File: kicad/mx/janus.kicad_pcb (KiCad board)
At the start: 2 copper layers, 95 x 95 mm, 62 parts, among them J1 8P8C Double Sided, SW1 SW_Push, SW10 SW_Push, SW11 SW_Push, SW12 SW_Push, SW13 SW_Push, SW14 SW_Push, SW15 SW_Push, SW16 SW_Push, SW17 SW_Push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

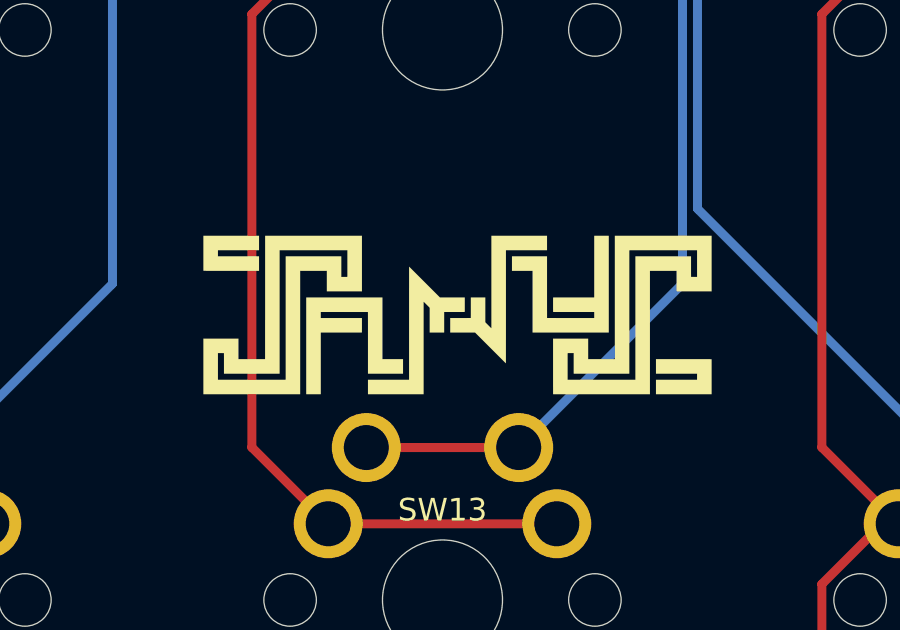
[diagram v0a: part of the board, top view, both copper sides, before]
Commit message: Center silkscreen logo
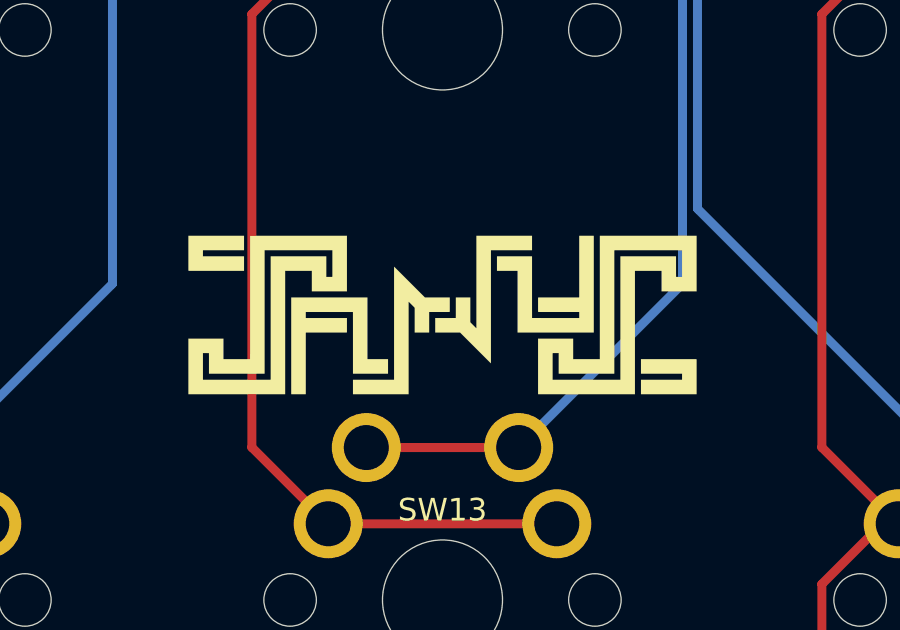
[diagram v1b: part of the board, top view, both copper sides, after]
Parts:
- moved LOGO1 0.50 mm to (148.5, 105.0)
- moved LOGO2 0.50 mm to (148.5, 105.0)
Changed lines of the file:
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@@
   )
   (footprint "janus-footprints:Logo_Janus" (layer "F.Cu")
-    (at 149 105 -45)
+    (at 148.5 105 -45)
     (property "Sheetfile" "janus.kicad_sch")
     (property "Sheetname" "")
@@
   )
   (footprint "janus-footprints:Logo_Janus" (layer "B.Cu")
-    (at 149 105 45)
+    (at 148.5 105 45)
     (property "Sheetfile" "janus.kicad_sch")
     (property "Sheetname" "")
